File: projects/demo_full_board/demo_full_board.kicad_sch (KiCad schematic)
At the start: 15 parts, among them U2 LM7805, Y1 16MHz

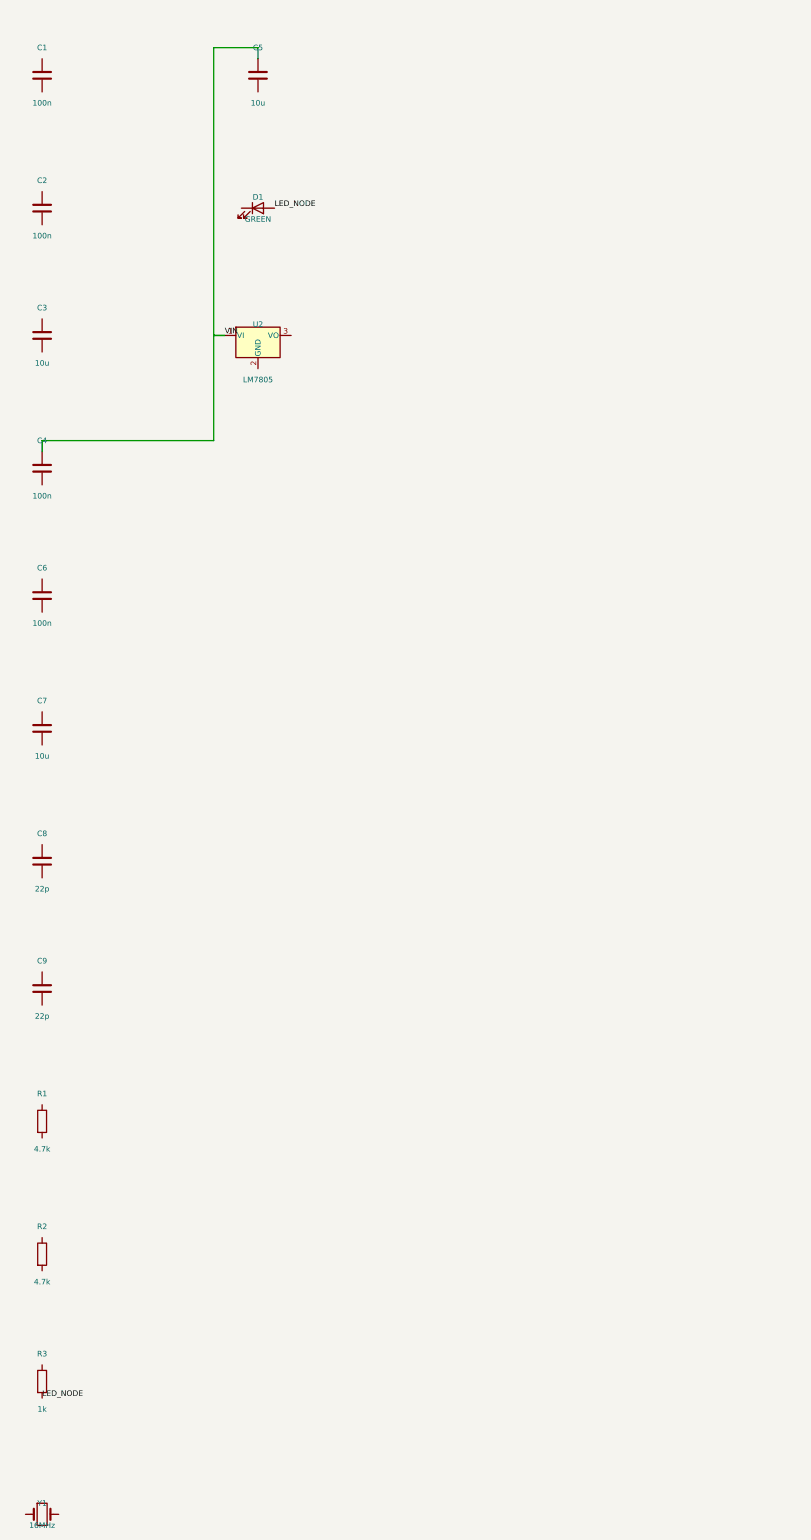
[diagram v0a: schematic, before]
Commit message: Phase 0: KiCad 10 migration + fix blind ERC parsing
- kicad-cli writes JSON reports only to -o file, never stdout; runner
  now uses a temp report file and real JSON decoding
- DetectKicadCLI exported and reused by render_sch and export_test
- KiCad 10 symbol renames (ATmega328-AU -> ATmega328-A) and pin
  numbers fixed in demos

Co-Authored-By: Claude Fable 5 <noreply@anthropic.com>
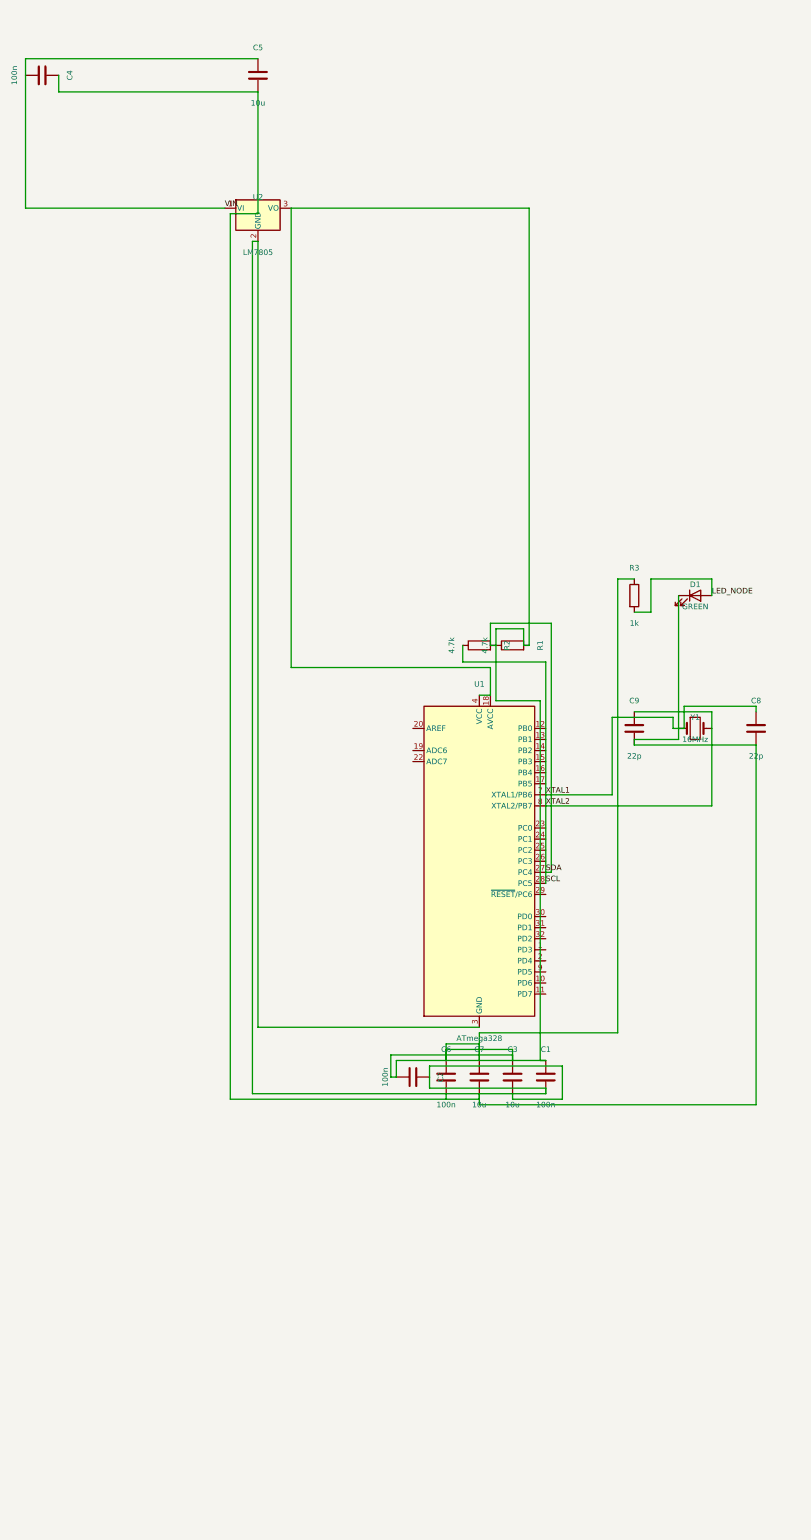
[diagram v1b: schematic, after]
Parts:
- added U1: ATmega328, symbol MCU_Microchip_ATmega:ATmega328-A
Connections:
- net SCL: now reaches C2.1
- net SCL: now also C1.1, C3.1, C6.1, C7.1, C8.1, C9.1, R1.1, R1.2, R2.1, R2.2, R3.1, U2.3 (VO), Y1.1, Y1.2, U1.18 (AVCC), U1.27 (PC4), U1.28 (PC5), U1.4 (VCC), U1.6 (VCC), U1.7 (XTAL1/PB6), U1.8 (XTAL2/PB7)
- net at C2.2: now also C1.2, C3.2, U2.2 (GND), U1.21 (GND), U1.3 (GND), U1.5 (GND)
- net at C5.2: now also C4.2, C6.2, C7.2, C8.2, C9.2, D1.1 (K)

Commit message: Phase 1: geometric quality gate (internal/place2/gate)
Post-hoc Enforce() guarantees zero cross-net crossings, zero wires
through symbol bodies, zero collinear overlaps: offending nets are
demoted to net labels (no geometry, identical connectivity). Wired
into connect_netlist and relayout. Same-net duplicate segments are
merged by Clean, not demoted.

Co-Authored-By: Claude Fable 5 <noreply@anthropic.com>
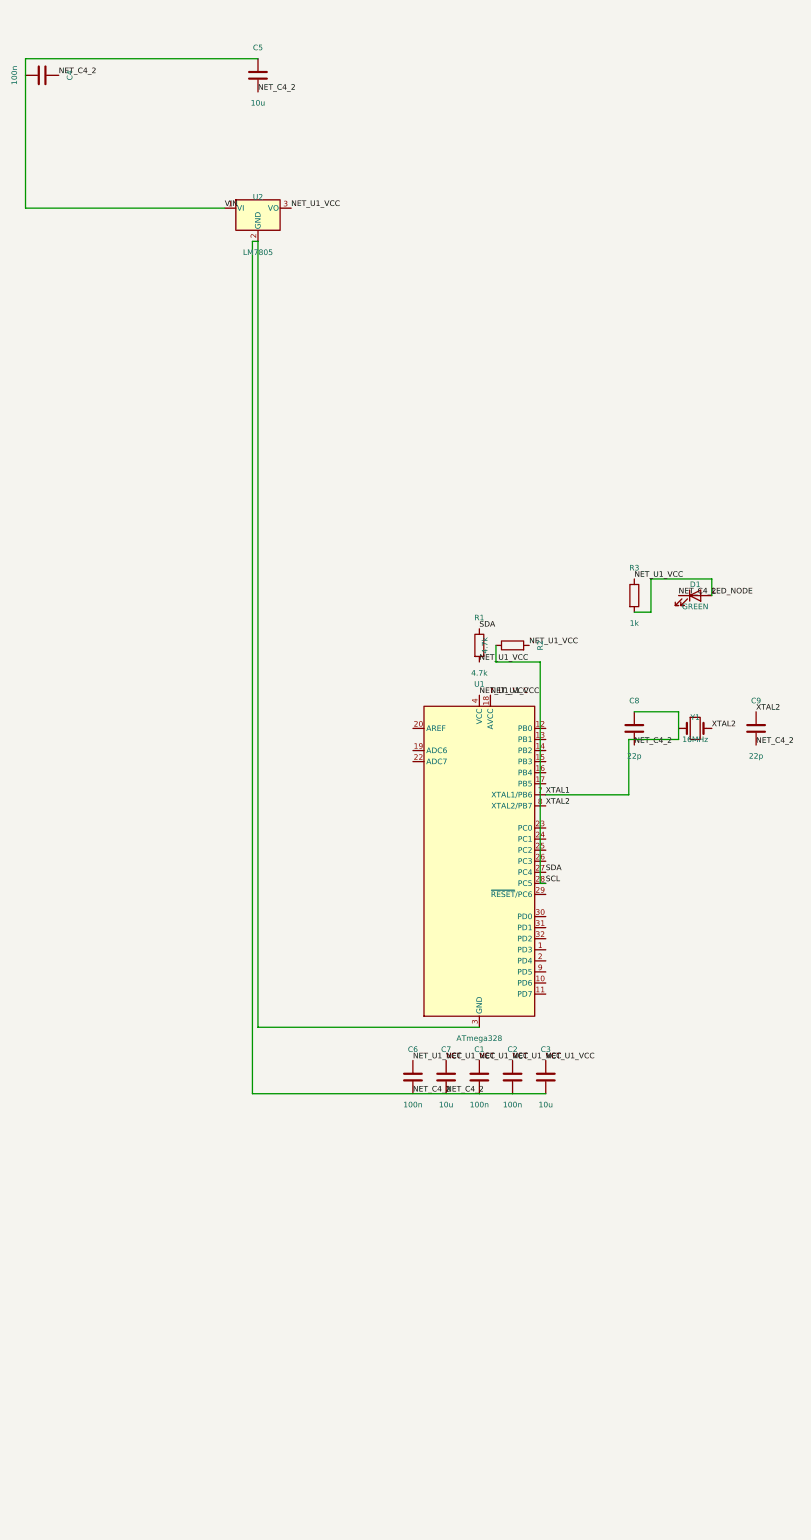
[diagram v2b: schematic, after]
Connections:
- net SCL: no longer C1.1, C2.1, C3.1, C6.1, C7.1, C8.1, C9.1, R1.1, R1.2, R2.2, R3.1, U1.18 (AVCC), U1.27 (PC4), U1.4 (VCC), U1.6 (VCC), U1.7 (XTAL1/PB6), U1.8 (XTAL2/PB7), U2.3 (VO), Y1.1, Y1.2
- net NET_C4_2: now reaches C4.2, C5.2, C6.2, C7.2, C8.2, C9.2, D1.1 (K)
- net NET_C4_2: now also C1.2, C2.2, C3.2, U1.21 (GND), U1.3 (GND), U1.5 (GND), U2.2 (GND)
- new net NET_U1_VCC: C1.1, C2.1, C3.1, C6.1, C7.1, R1.2, R2.2, R3.1, U1.18 (AVCC), U1.4 (VCC), U1.6 (VCC), U2.3 (VO)
- new net SDA: R1.1, U1.27 (PC4)
- new net XTAL1: C8.1, U1.7 (XTAL1/PB6), Y1.1
- new net XTAL2: C9.1, U1.8 (XTAL2/PB7), Y1.2

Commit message: Phase 3: parametric cluster wiring generators (internal/place2/wiregen)
Closed-form wiring (straight or single-L with clear-corridor
preconditions) for decoupling, 2-pin satellites, dividers and crystal
load caps; generators apply or decline, never search. Integrated as a
pre-pass in connect_netlist with component-aware MST; discovery-label
fallback now also fires for nets fully consumed by wiregen (fixes
dropped-net regression, covered by two regression tests).

Co-Authored-By: Claude Fable 5 <noreply@anthropic.com>
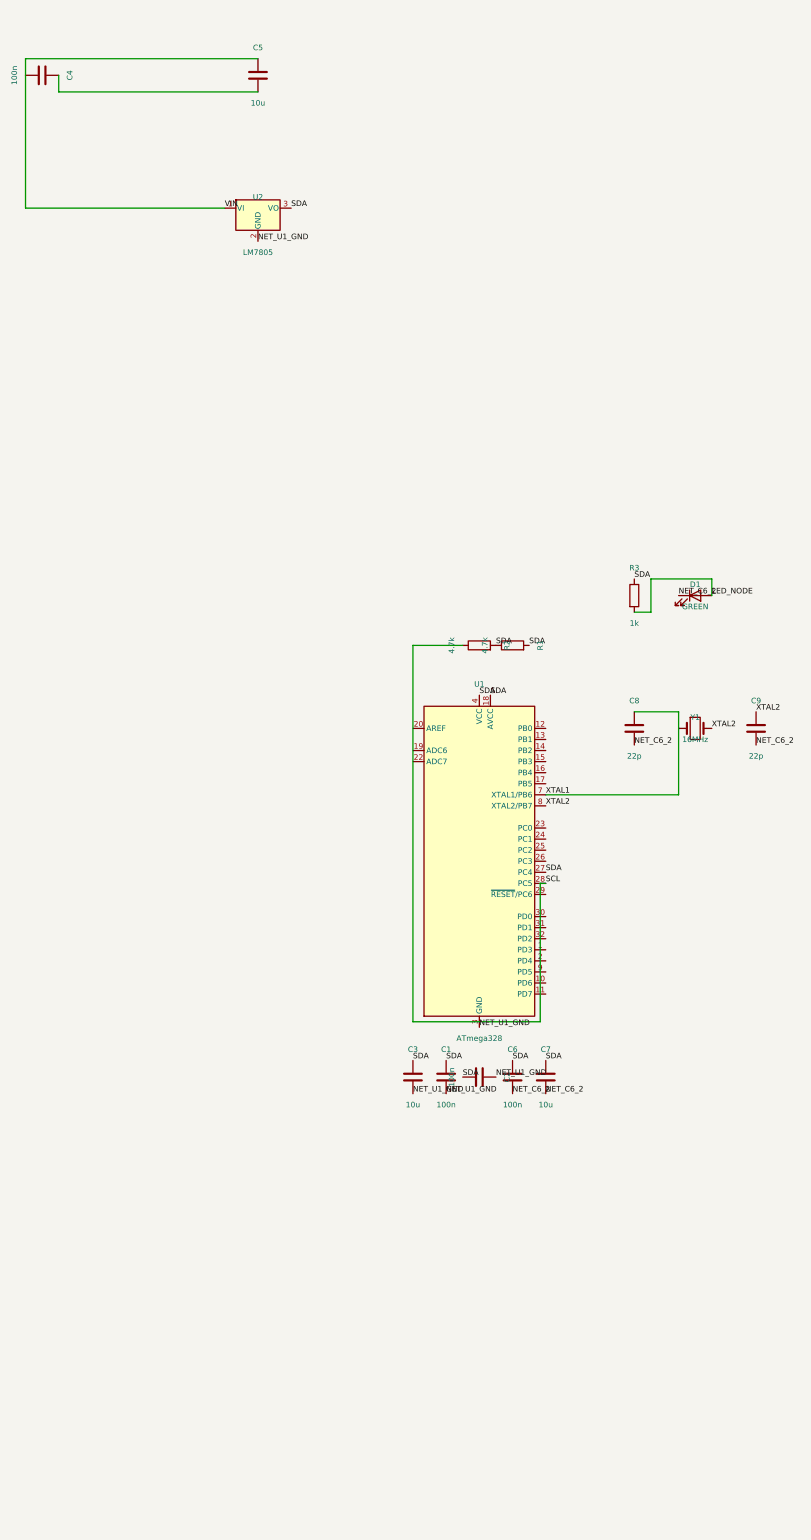
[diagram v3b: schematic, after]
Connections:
- net NET_U1_VCC is gone; now on net SDA: C1.1, C2.1, C3.1, C6.1, C7.1, R1.2, R2.2, R3.1, U1.18 (AVCC), U1.4 (VCC), U1.6 (VCC), U2.3 (VO)
- net NET_C4_2 renamed NET_U1_GND
- net NET_U1_GND: no longer C4.2, C5.2, C6.2, C7.2, C8.2, C9.2, D1.1 (K)
- new net: C4.2, C5.2
- new net NET_C6_2: C6.2, C7.2, C8.2, C9.2, D1.1 (K)

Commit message: Phase 4: per-pin power rail policy + full pipeline determinism
Power nets are never routed: every pin on a rail gets its own power
symbol (GND down, VCC up) with a 2.54mm stub; PWR_FLAG emitted after
the gate for undriven power_in nets. Determinism: cluster detection
and TraceNets no longer depend on Go map iteration order (refOrder
slices, sorted canonical net naming). 6/6 identical runs on vreg and
mcu demos; vreg ERC now has zero errors.

Co-Authored-By: Claude Fable 5 <noreply@anthropic.com>
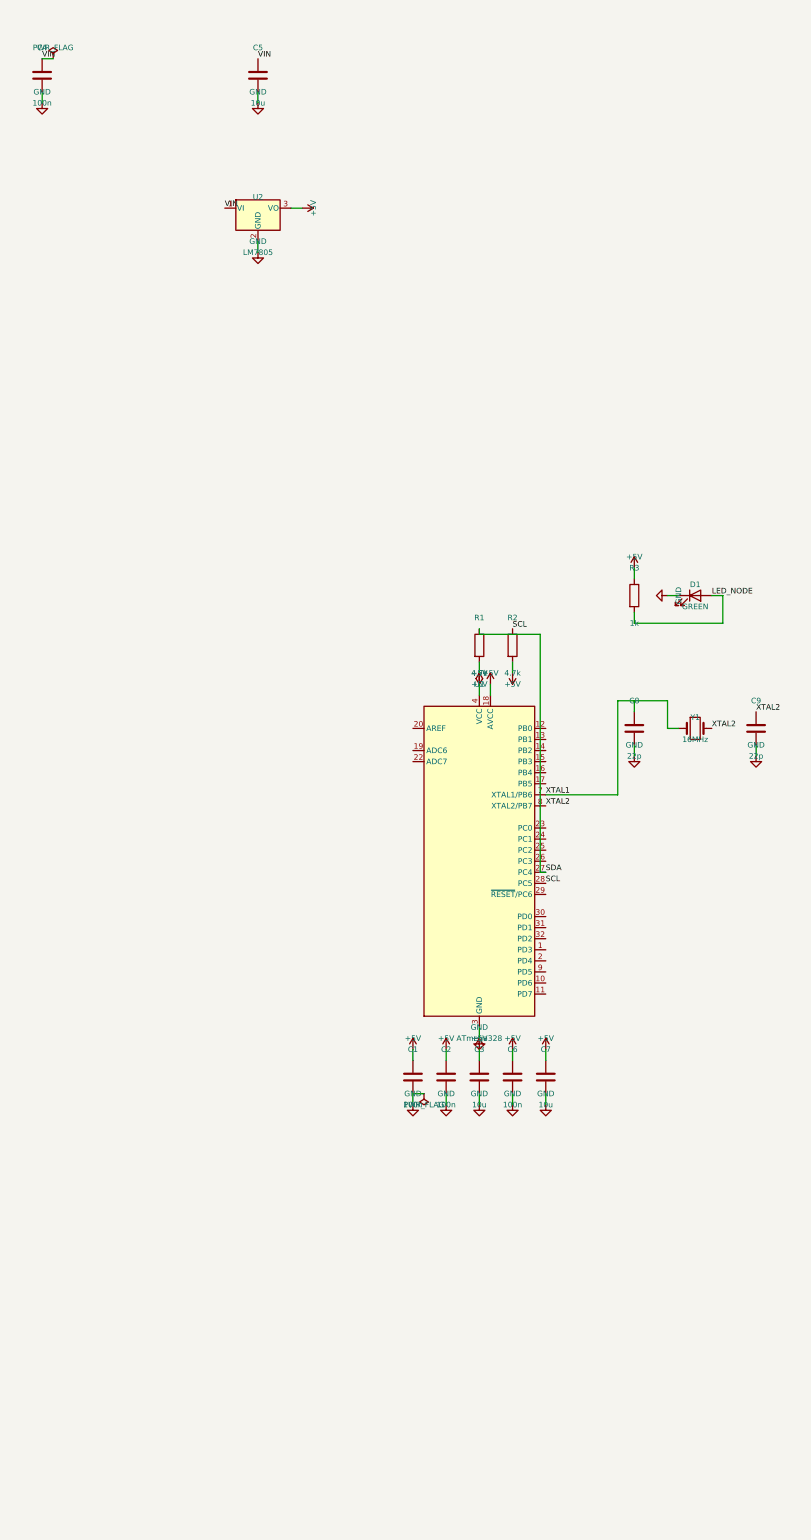
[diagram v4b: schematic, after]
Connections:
- net NET_C6_2 is gone; now on net GND: C6.2, C7.2, C8.2, C9.2, D1.1 (K)
- net NET_U1_GND is gone; now on net GND: C1.2, C2.2, C3.2, U1.21 (GND), U1.3 (GND), U1.5 (GND), U2.2 (GND)
- net SDA: no longer C1.1, C2.1, C3.1, C6.1, C7.1, R1.2, R2.2, R3.1, U1.18 (AVCC), U1.4 (VCC), U1.6 (VCC), U2.3 (VO)
- net GND: now reaches C4.2, C5.2
- new net +5V: C1.1, C2.1, C3.1, C6.1, C7.1, R1.2, R2.2, R3.1, U1.18 (AVCC), U1.4 (VCC), U1.6 (VCC), U2.3 (VO)

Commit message: Phase 4b: fit schematic content to sheet after relayout
Rigid grid-aligned translation of all content into the usable page
area (>=12.7mm margins), avoiding the title block; auto-upgrades
paper A4->A3 when content cannot fit. Known limit: mcu_i2c PlaceFlow
column sprawl (302mm) exceeds A3; placement compaction pending.

Co-Authored-By: Claude Fable 5 <noreply@anthropic.com>
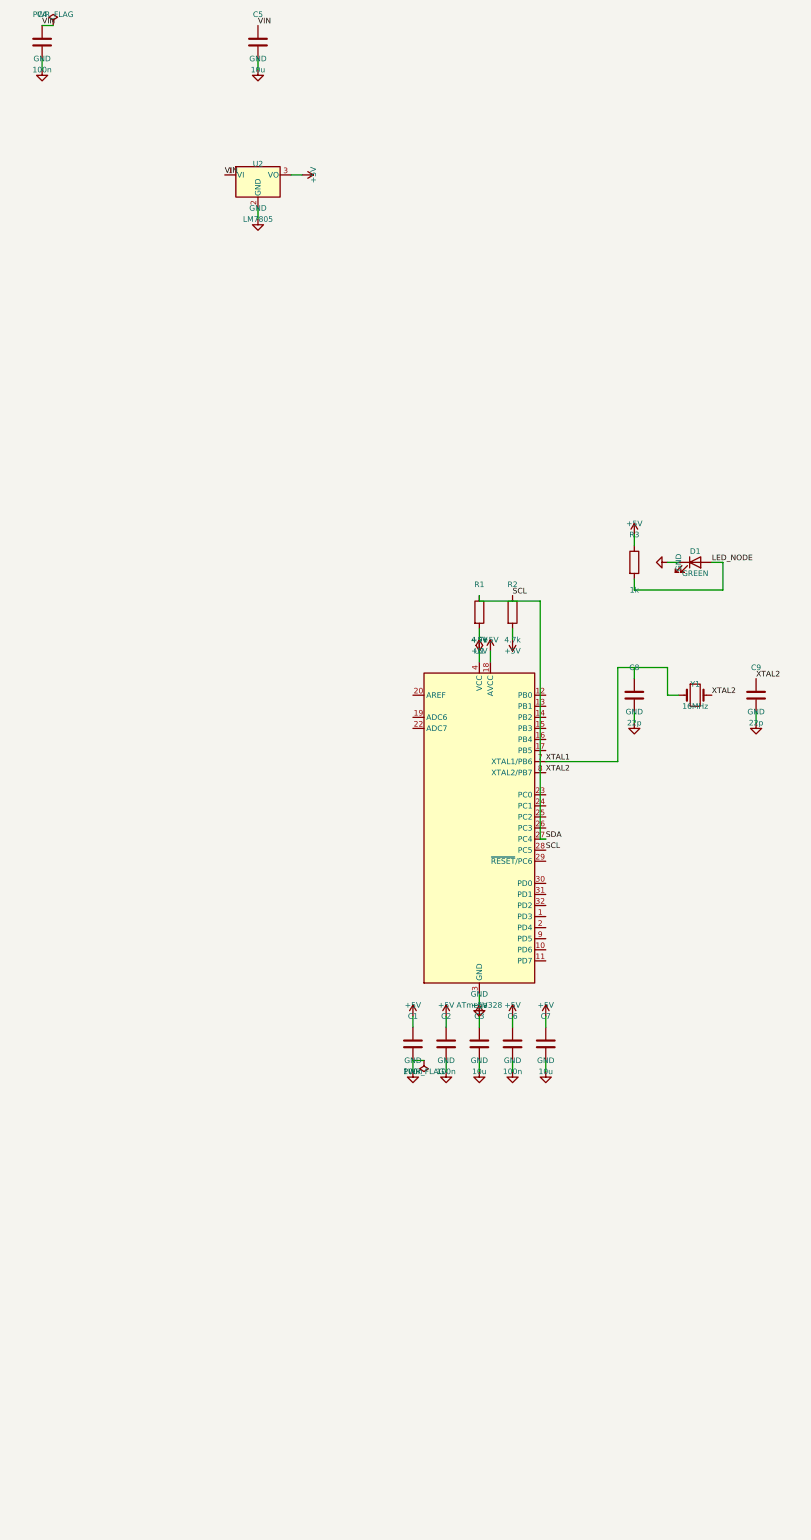
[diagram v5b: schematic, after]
